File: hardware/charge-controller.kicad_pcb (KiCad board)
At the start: 2 copper layers, 87.5 x 53 mm, 47 parts, among them J1 Conn_02x04_Odd_Even, J2 Conn_02x03_Odd_Even, J4 CAN_TERM, Q1 MMBT3904, Q2 NCV8402xST, Q3 NCV8402xST, Q4 NCV8402xST, Q5 NCV8402xST, U1 Pico, U2 MCP2515-xST, U3 SN65HVD230, U4 TPS62160DGK

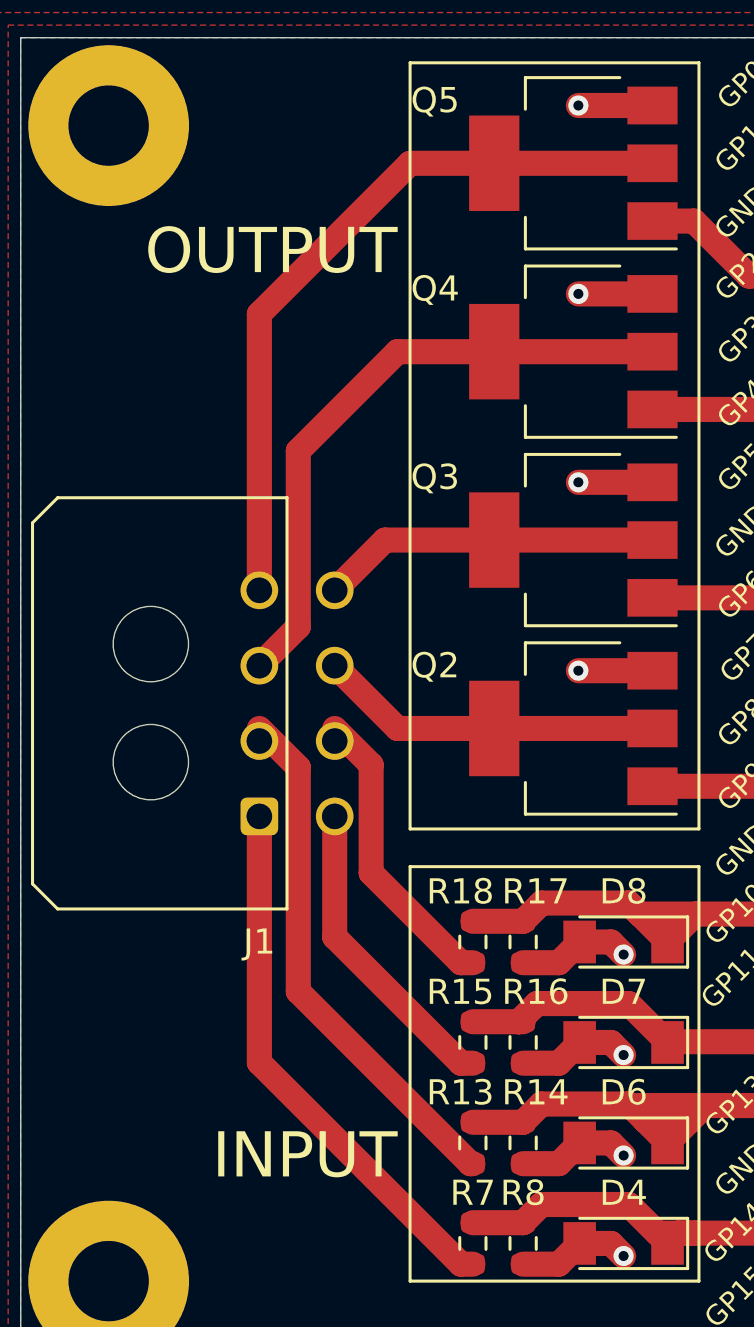
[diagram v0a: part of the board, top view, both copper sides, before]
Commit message: tidy up traces
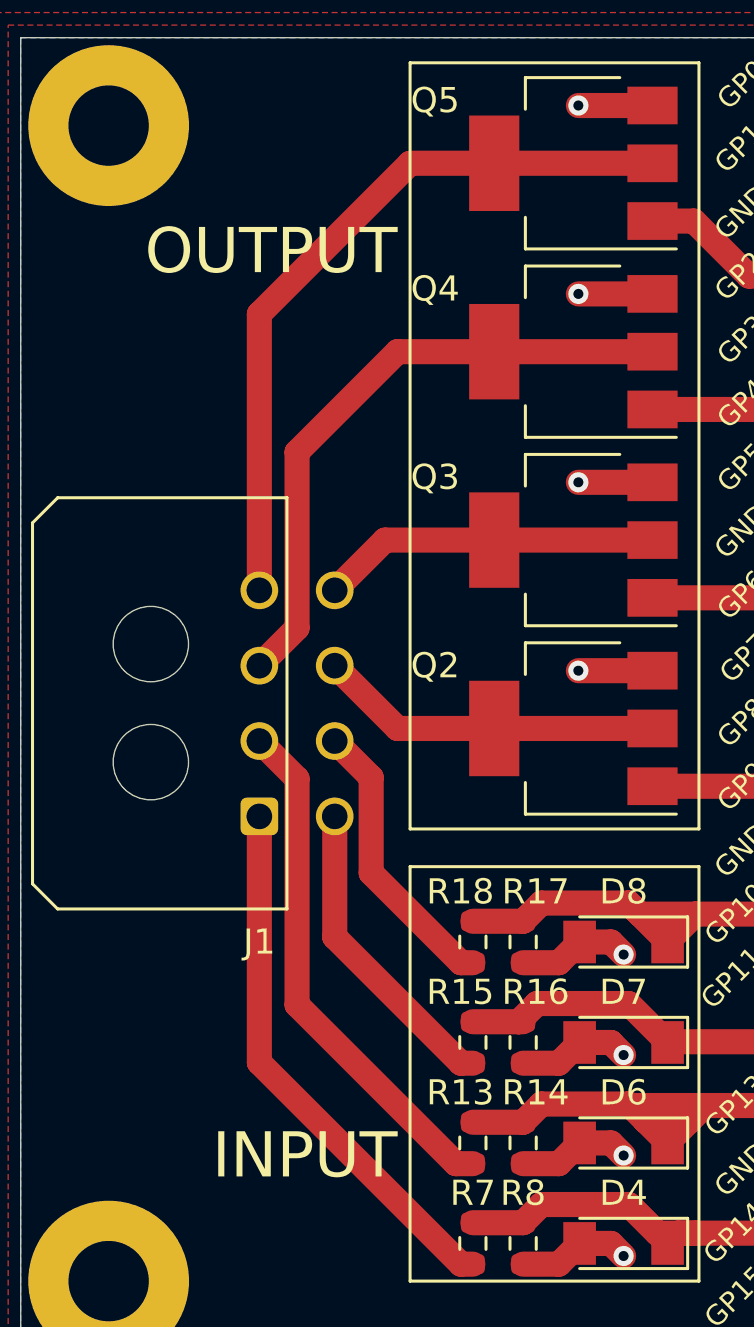
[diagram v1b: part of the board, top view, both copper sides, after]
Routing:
- net IN12_4: track 11.9 -> 11.4 mm

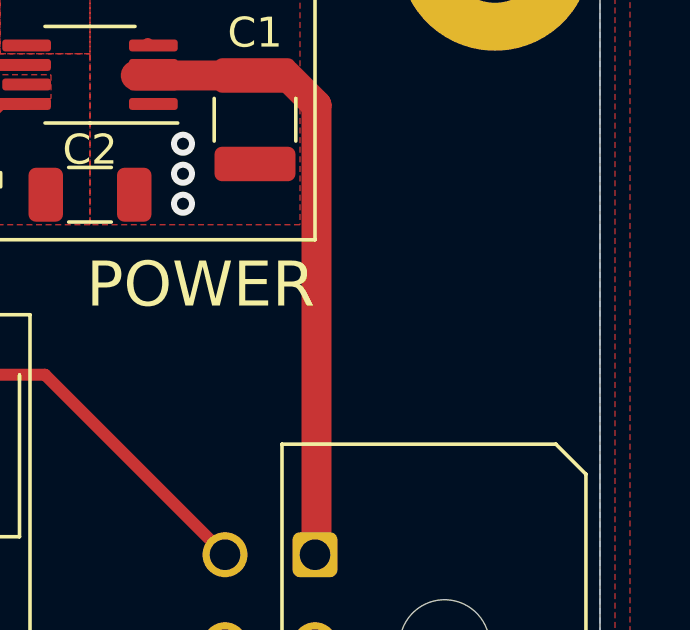
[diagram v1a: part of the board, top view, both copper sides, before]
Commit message: add logo
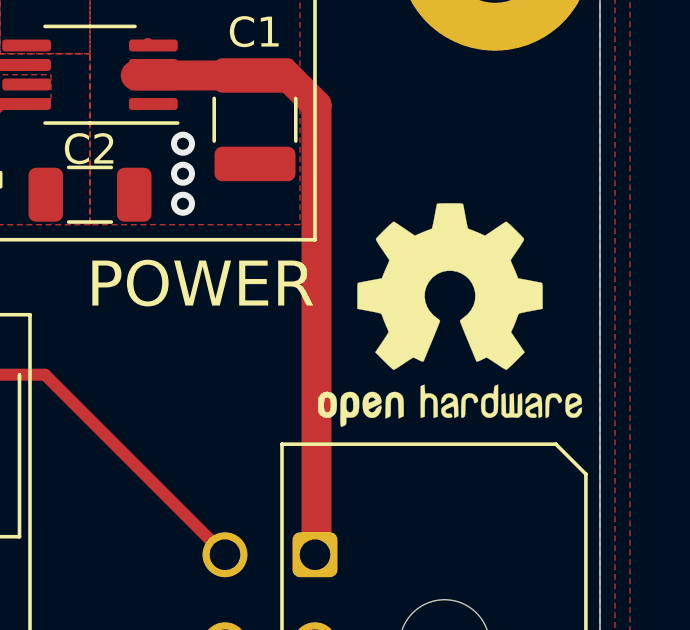
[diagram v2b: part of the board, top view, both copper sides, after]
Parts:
- added REF**: OSHW-Logo2_9.8x8mm_SilkScreen, Symbol:OSHW-Logo2_9.8x8mm_SilkScreen, F.Cu at (171.5, 77.5)

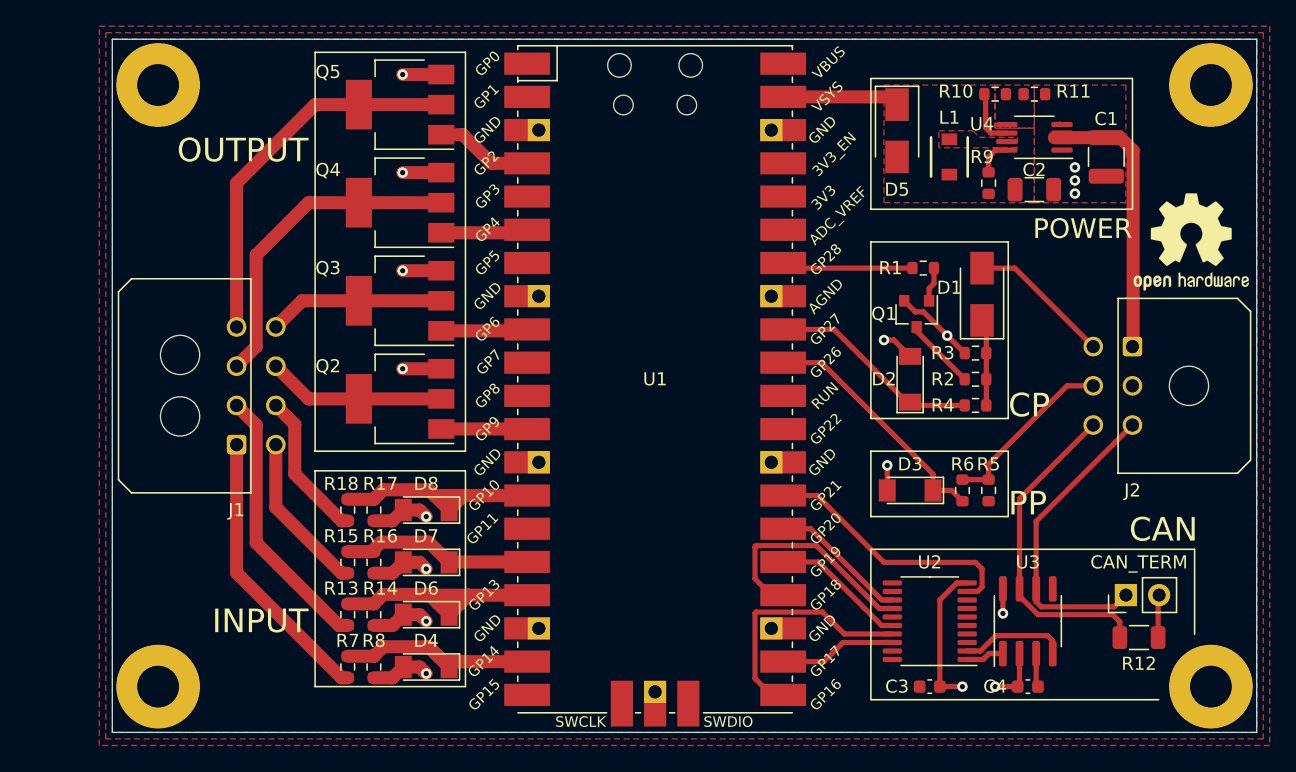
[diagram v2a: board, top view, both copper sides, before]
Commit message: improve 12v inputs, connect CAN line driver sleep pin
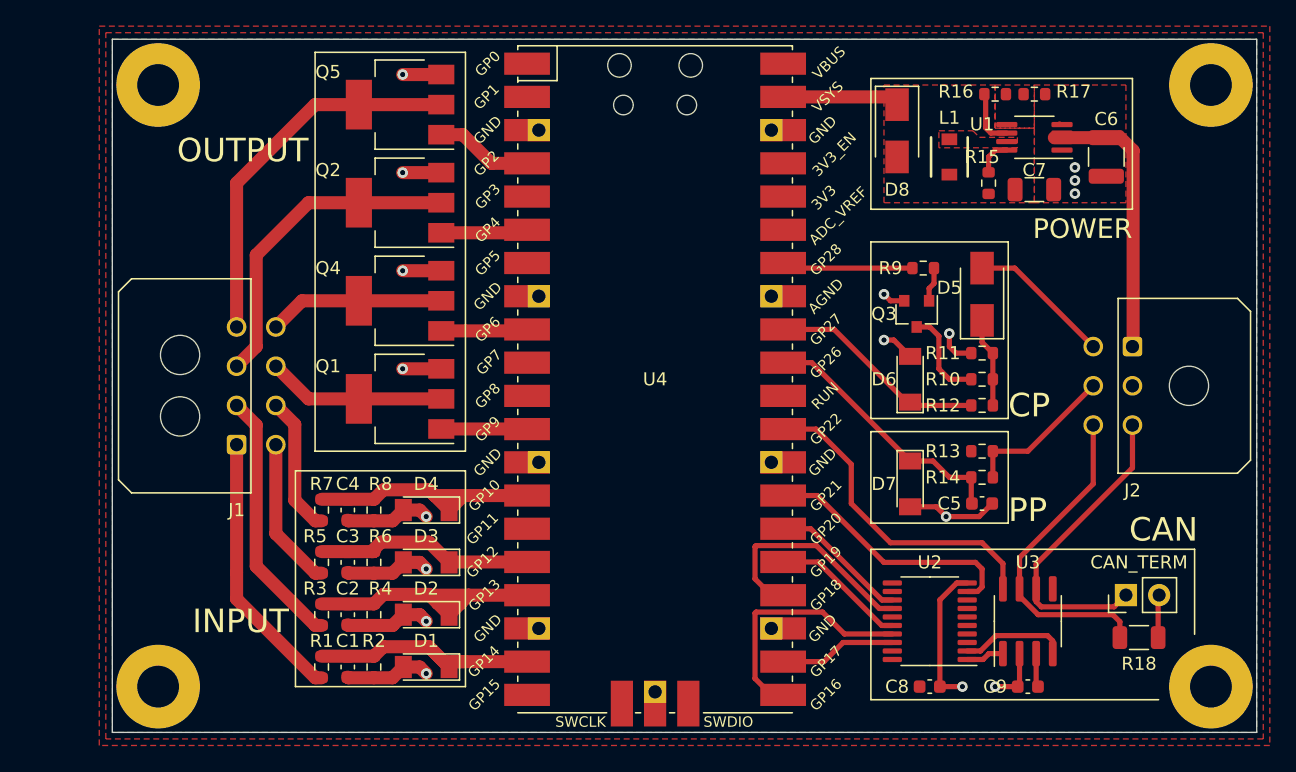
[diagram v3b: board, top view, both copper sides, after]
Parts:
- removed the D3 at (150.0, 96.5)
- removed the R13 at (107.0, 106.0)
- removed the R6 at (154.0, 96.5)
- removed REF**: OSHW-Logo2_9.8x8mm_SilkScreen, Symbol:OSHW-Logo2_9.8x8mm_SilkScreen
- added C1: 470n, Capacitor_SMD:C_0603_1608Metric, F.Cu at (107.0, 110.0)
- added C2: 470n, Capacitor_SMD:C_0603_1608Metric, F.Cu at (107.0, 106.0)
- added C3: 470n, Capacitor_SMD:C_0603_1608Metric, F.Cu at (107.0, 102.0)
- added C4: 470n, Capacitor_SMD:C_0603_1608Metric, F.Cu at (107.0, 98.0)
- added C5: 470n, Capacitor_SMD:C_0603_1608Metric, F.Cu at (155.5, 97.5)
- added D7: 3v, Diode_SMD:D_MiniMELF, F.Cu at (150.0, 96.0)
- added R14: 47k, Resistor_SMD:R_0603_1608Metric, F.Cu at (155.5, 95.5)
- added R3: 4k7, Resistor_SMD:R_0603_1608Metric, F.Cu at (105.0, 106.0)
- R1: renamed from R7; value 5k6 -> 4k7
- R5: renamed from R15; value 5k6 -> 4k7
- R7: renamed from R17; value 5k6 -> 4k7
- moved R13 3.04 mm to (155.5, 93.5), turned to 0 degrees
- moved R1 2.00 mm to (105.0, 110.0)
- moved R5 2.00 mm to (105.0, 102.0)
- moved R7 2.00 mm to (105.0, 98.0)
- moved R10 0.50 mm to (155.5, 88.0)
- moved R11 0.50 mm to (155.5, 86.0)
- moved R12 0.50 mm to (155.5, 90.0)
- renumbered C1 to C6, C2 to C7, C3 to C8, C4 to C9, D4 to D1, D6 to D2, D7 to D3, D8 to D4, D1 to D5, D2 to D6, D5 to D8, J4 to J3, Q2 to Q1, Q4 to Q2, Q1 to Q3, Q3 to Q4, R2 to R10, R3 to R11, R4 to R12, R5 to R13, R9 to R15, R10 to R16, R11 to R17, R12 to R18, R8 to R2, R14 to R4, R16 to R6, R18 to R8, R1 to R9, U4 to U1, U1 to U4
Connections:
- U3 pad 8: GND -> Rs
- U4 pad 29: (no net) -> Rs
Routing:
- net Rs: track 0.00 -> 25.7 mm
- net GND: track 57.9 -> 67.6 mm
- net IN3: track 15.7 -> 17.9 mm
- net IN4: track 18.9 -> 20.9 mm
- net IN2: track 21.0 -> 23.0 mm
- net IN1: track 18.9 -> 20.9 mm
- net EVSE_PP: track 13.7 -> 11.7 mm
- net Net-(Q3-Pad3): track 5.52 -> 7.30 mm
- net MCU_PP: track 19.7 -> 20.9 mm
- net IN12_2: track 20.7 -> 19.8 mm
- net IN12_3: track 12.4 -> 11.6 mm
- net IN12_1: track 21.6 -> 20.8 mm
- net IN12_4: track 11.4 -> 10.6 mm
- net Net-(D5-Pad1): track 6.63 -> 7.30 mm
- net MCU_CP: track 17.2 -> 17.7 mm

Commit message: v3
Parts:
- added REF**: OSHW-Logo2_24.3x20mm_SilkScreen, Symbol:OSHW-Logo2_24.3x20mm_SilkScreen, B.Cu at (130.5, 90.0)
- moved J1 7.00 mm to (91.5, 93.0)
- moved H1 6.50 mm to (86.0, 65.5)
- moved H3 6.50 mm to (86.0, 111.5)
- moved C1 2.50 mm to (104.5, 110.0)
- moved C2 2.50 mm to (104.5, 106.0)
- moved C3 2.50 mm to (104.5, 102.0)
- moved C4 2.50 mm to (104.5, 98.0)
- moved D1 2.50 mm to (110.5, 110.0)
- moved D2 2.50 mm to (110.5, 106.0)
- moved D3 2.50 mm to (110.5, 102.0)
- moved D4 2.50 mm to (110.5, 98.0)
- moved Q1 2.50 mm to (108.5, 89.5)
- moved Q2 2.50 mm to (108.5, 74.5)
- moved Q4 2.50 mm to (108.5, 82.0)
- moved Q5 2.50 mm to (108.5, 67.0)
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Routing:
- net OUT12_2: track 13.5 -> 18.0 mm
- net OUT12_1: track 13.3 -> 17.8 mm
- net IN2: track 23.0 -> 25.5 mm
- net OUT4: track 8.37 -> 10.9 mm
- net OUT3: track 7.56 -> 10.1 mm
- net OUT2: track 7.51 -> 10.0 mm
- net IN4: track 20.9 -> 23.4 mm
- net IN3: track 17.9 -> 20.4 mm
- net OUT1: track 7.46 -> 9.96 mm
- net IN12_2: track 19.8 -> 21.7 mm
- net IN12_3: track 11.6 -> 13.4 mm
- net IN12_1: track 20.8 -> 22.7 mm
- net IN12_4: track 10.6 -> 12.4 mm
- net OUT12_4: track 28.8 -> 30.6 mm
- net OUT12_3: track 24.6 -> 26.2 mm
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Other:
- board size 87.5 x 53 mm -> 93.5 x 53 mm
- board text added: "Charge Conteoller v3"

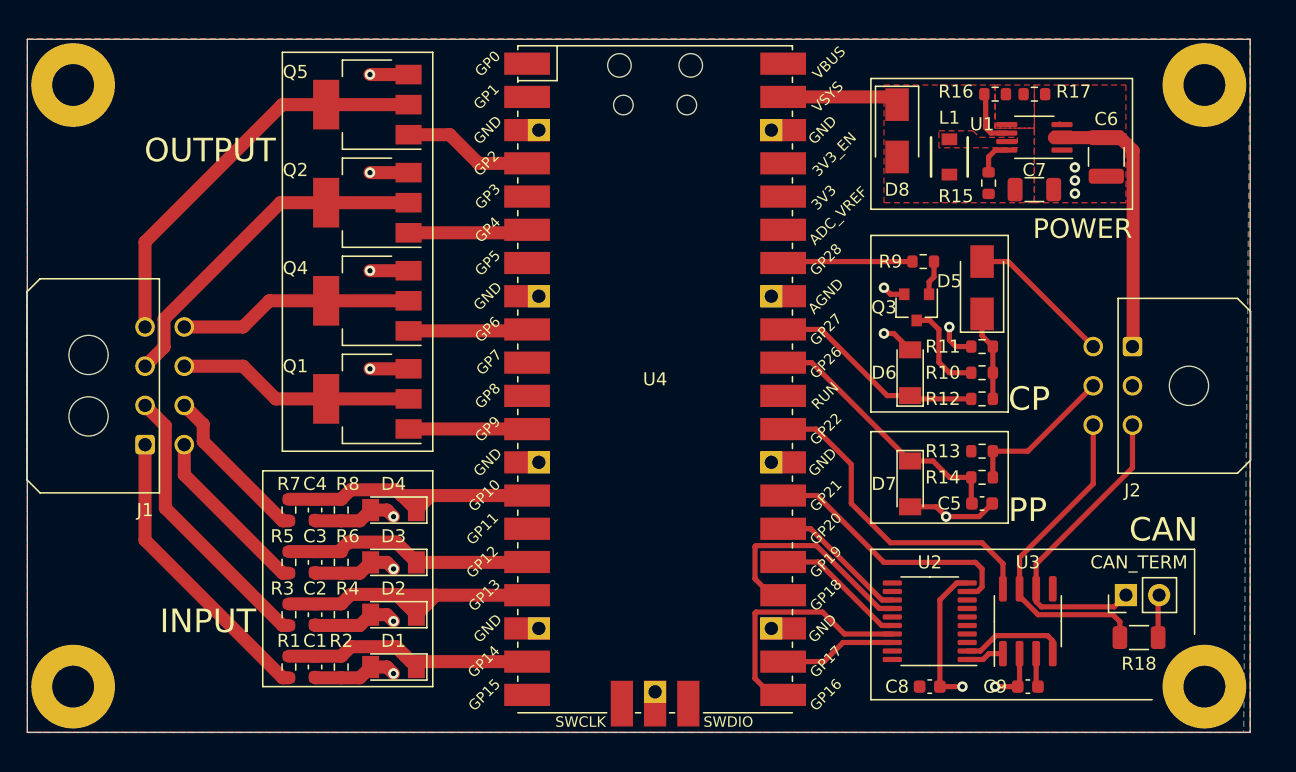
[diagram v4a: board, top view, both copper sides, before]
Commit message: update schematic and picture
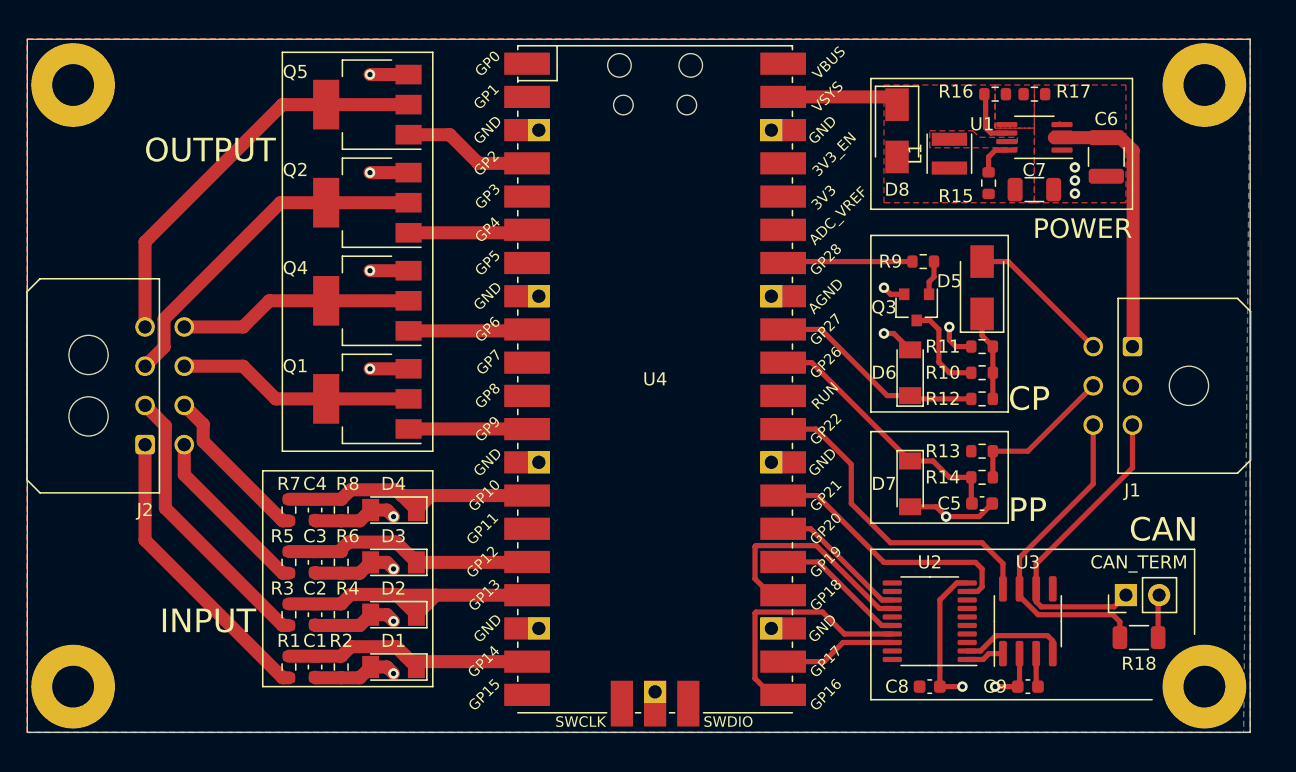
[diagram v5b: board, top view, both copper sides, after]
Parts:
- removed REF**: OSHW-Logo2_24.3x20mm_SilkScreen, Symbol:OSHW-Logo2_24.3x20mm_SilkScreen
- C1, C2, C3, C4, C5: value 470n -> 1u
- L1: footprint footprints:1227ASH100MP2 -> Inductor_SMD:L_Neosid_SMS-ME3015
- moved L1 0.25 mm to (153.0, 70.8)
- renumbered J2 to J1, J1 to J2

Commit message: rework inuts
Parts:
- removed the D6 at (150.0, 87.5)
- removed D7: 3v, Diode_SMD:D_MiniMELF
- removed the Q3 at (150.5, 82.5)
- removed the R13 at (155.5, 93.5)
- removed the R16 at (156.5, 66.2)
- added Q5: MMBT3904, Package_TO_SOT_SMD:SOT-23, F.Cu at (150.5, 83.5)
- added Q6: MMBT3904, Package_TO_SOT_SMD:SOT-23, F.Cu at (150.5, 88.0)
- C1, C2, C3, C4: value 1u -> 100n
- D1, D2, D3, D4: value 3v -> 3.3v
- R1, R3, R5, R7: value 4k7 -> 47k
- R12: value 47k -> 330
- R14: value 47k -> 220k
- R2, R4, R6, R8: value 1k5 -> 4.7k
- R9: value 2k7 -> 1k5
- moved R14 29.3 mm to (156.5, 66.2), turned to 0 degrees
- moved R12 8.51 mm to (149.0, 95.0), turned to 90 degrees
- moved C5 4.30 mm to (152.0, 95.0), turned to 270 degrees
- moved R10 2.69 mm to (154.5, 85.0)
- moved R11 2.69 mm to (154.5, 88.0), turned to 180 degrees
- moved C1 2.00 mm to (106.5, 110.0)
- moved C2 2.00 mm to (106.5, 106.0)
- moved C3 2.00 mm to (106.5, 102.0)
- moved C4 2.00 mm to (106.5, 98.0)
- moved R2 2.00 mm to (104.5, 110.0), turned to 270 degrees
- moved R4 2.00 mm to (104.5, 106.0), turned to 270 degrees
- moved R6 2.00 mm to (104.5, 102.0), turned to 270 degrees
- moved R8 2.00 mm to (104.5, 98.0), turned to 270 degrees
- moved R9 1.50 mm to (149.5, 79.0), turned to 0 degrees
- moved D5 0.50 mm to (155.5, 80.5)
- renumbered D8 to D6, J2 to J1, J1 to J2, Q4 to Q2, Q2 to Q3, Q5 to Q4, R15 to R13, R17 to R15, R18 to R16, U4 to U2, U2 to U3, U3 to U4
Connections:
- C5 pad 1: MCU_PP -> EVSE_PP
- R1 pad 1: IN1 -> IN12_1
- R1 pad 2: IN12_1 -> GND
- R11 pad 1: GND -> Net-(D5-Pad1)
- R11 pad 2: Net-(D5-Pad1) -> Net-(Q6-Pad1)
- R12 pad 1: MCU_CP -> +3V3
- R12 pad 2: Net-(D5-Pad1) -> EVSE_PP
- R14 pad 1: EVSE_PP -> +5V
- R14 pad 2: MCU_PP -> Net-(R14-Pad2)
- R15 pad 1: Net-(R16-Pad2) -> Net-(R14-Pad2)
- R2 pad 1: GND -> IN12_1
- R3 pad 1: IN2 -> IN12_2
- R3 pad 2: IN12_2 -> GND
- R4 pad 1: GND -> IN12_2
- R5 pad 1: IN3 -> IN12_3
- R5 pad 2: IN12_3 -> GND
- R6 pad 1: GND -> IN12_3
- R7 pad 1: IN4 -> IN12_4
- R7 pad 2: IN12_4 -> GND
- R8 pad 1: GND -> IN12_4
- R9 pad 1: Net-(Q3-Pad1) -> MCU_SW
- R9 pad 2: MCU_SW -> Net-(Q5-Pad1)
- U1 pad 5: Net-(R16-Pad2) -> Net-(R14-Pad2)
- U2 pad 31: MCU_PP -> EVSE_PP
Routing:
- net MCU_PP: track 20.9 -> 0.00 mm
- net EVSE_PP: track 11.7 -> 30.8 mm
- net IN2: track 25.5 -> 19.3 mm
- net MCU_CP: track 17.5 -> 13.1 mm
- net IN4: track 23.4 -> 19.1 mm
- net Net-(Q5-Pad1): track 0.00 -> 3.97 mm
- net Net-(Q5-Pad3): track 7.30 -> 3.38 mm
- net IN1: track 22.1 -> 18.8 mm
- net Net-(Q3-Pad1): track 2.66 -> 0.00 mm
- net Net-(Q6-Pad1): track 0.00 -> 2.64 mm
- net IN3: track 20.4 -> 18.7 mm
- net Net-(D5-Pad1): track 7.30 -> 5.57 mm
- net MCU_SW: track 10.8 -> 9.33 mm
- net GND: track 67.6 -> 66.1 mm, vias 17 -> 16
- net IN12_4: track 12.4 -> 13.0 mm
- added copper zone on F.Cu, net Net-(R14-Pad2)
- removed copper zone on F.Cu, net Net-(R16-Pad2)
